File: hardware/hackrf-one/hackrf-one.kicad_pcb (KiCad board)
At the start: 4 copper layers, 120 x 75 mm, 432 parts, among them J1 USB-MICRO-B, J10 GND_CLIP, J2 RF-SHIELD-FRAME, J3 RF-SHIELD-COVER, J4 MOUNTING_HOLE, J5 MOUNTING_HOLE, J6 MOUNTING_HOLE, J7 MOUNTING_HOLE, J8 MOUNTING_HOLE, J9 MOUNTING_HOLE, P1 1V8, P13 GPO1, P14 XCVR_CLKOUT, P15 INTR, P16 CLKIN, P17 GPO6, P18 OEB, P19 GPO3, P2 CLKOUT, P20 GPIO, P21 REF_IN, P22 I2S, P23 DBGEN, P24 TRST, P25 LPC_ISP, P26 LPC_JTAG, P27 MIXER_SDATA, P28 SD, P29 CPLD_JTAG, P3 GND, P30 BANK2_AUX, P31 MIXER_SCLK, P32 MIXER_ENX, P33 MIXER_RESETX, P34 MIX_BYPASS, P35 !MIX_BYPASS, P36 VAA, P37 SCL, P38 SDA, P39 SSP1_SCK, P4 ANTENNA, P40 SSP1_MOSI, P41 SSP1_MISO, P42 TX, P43 RX, P44 HP, P45 LP, P46 TX_MIX_BP, P47 RX_MIX_BP, P48 TX_AMP, P49 RX_AMP, P5 LEDS, P50 AMP_BYPASS, P51 !TX_AMP_PWR, P52 !RX_AMP_PWR, P53 CS_XCVR, P54 CS_AD, P55 TXENABLE, P56 RXENABLE, P57 XTAL2, P58 GCK1, P59 GCK2, P6 GPO4, P60 SGPIO_CLK, P61 DA0, P62 DA7, P63 DD0, P64 DD9, P65 DA4, P66 DD5, P67 RSSI, P68 SPIFI_CS, P69 VREGMODE, P7 GPO2, P70 EN_1V8, P71 ID, P72 GP_CLKIN, P73 P1_2, P74 P1_1, P75 GP_CLKIN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

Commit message: adopt OSHWA convention for SPI signal names
https://www.oshwa.org/a-resolution-to-redefine-spi-signal-names
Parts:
- P40: value SSP1_MOSI -> SSP1_COPI
- P41: value SSP1_MISO -> SSP1_CIPO
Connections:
- net /mcu/usb/power/SPIFI_MISO renamed /mcu/usb/power/SPIFI_CIPO
- net /mcu/usb/power/SPIFI_MOSI renamed /mcu/usb/power/SPIFI_COPI
- net SSP1_MISO renamed SSP1_CIPO
- net SSP1_MOSI renamed SSP1_COPI
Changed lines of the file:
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@@
   (net 145 /mcu/usb/power/SGPIO9)
   (net 146 /mcu/usb/power/SPIFI_CS)
-  (net 147 /mcu/usb/power/SPIFI_MISO)
-  (net 148 /mcu/usb/power/SPIFI_MOSI)
+  (net 147 /mcu/usb/power/SPIFI_CIPO)
+  (net 148 /mcu/usb/power/SPIFI_COPI)
   (net 149 /mcu/usb/power/SPIFI_SCK)
   (net 150 /mcu/usb/power/SPIFI_SIO2)
@@
   (net 210 SDA)
   (net 211 SGPIO_CLK)
-  (net 212 SSP1_MISO)
-  (net 213 SSP1_MOSI)
+  (net 212 SSP1_CIPO)
+  (net 213 SSP1_COPI)
   (net 214 SSP1_SCK)
   (net 215 TX)
@@
     (add_net /mcu/usb/power/SGPIO9)
     (add_net /mcu/usb/power/SPIFI_CS)
-    (add_net /mcu/usb/power/SPIFI_MISO)
-    (add_net /mcu/usb/power/SPIFI_MOSI)
+    (add_net /mcu/usb/power/SPIFI_CIPO)
+    (add_net /mcu/usb/power/SPIFI_COPI)
     (add_net /mcu/usb/power/SPIFI_SCK)
     (add_net /mcu/usb/power/SPIFI_SIO2)
@@
     (add_net SDA)
     (add_net SGPIO_CLK)
-    (add_net SSP1_MISO)
-    (add_net SSP1_MOSI)
+    (add_net SSP1_CIPO)
+    (add_net SSP1_COPI)
     (add_net SSP1_SCK)
     (add_net TX)
@@
       (net 193 GND) (solder_mask_margin 0.1016))
     (pad 1 smd rect (at -0.5334 0 180) (size 0.508 0.5588) (layers C1F F.Paste F.Mask)
-      (net 212 SSP1_MISO) (die_length -2147.483648) (solder_mask_margin 0.1016))
+      (net 212 SSP1_CIPO) (die_length -2147.483648) (solder_mask_margin 0.1016))
   )
   (module hackrf:GSG-0402 (layer C1F)
@@
       (net 99 /mcu/usb/power/I2C1_SDA) (die_length 0.12192))
     (pad 7 thru_hole circle (at -7.62 1.27 180) (size 1.524 1.524) (drill 1.016) (layers *.Cu *.Mask F.SilkS)
-      (net 147 /mcu/usb/power/SPIFI_MISO) (die_length 0.12192))
+      (net 147 /mcu/usb/power/SPIFI_CIPO) (die_length 0.12192))
     (pad 8 thru_hole circle (at -7.62 -1.27 180) (size 1.524 1.524) (drill 1.016) (layers *.Cu *.Mask F.SilkS)
       (net 149 /mcu/usb/power/SPIFI_SCK) (die_length 0.08382))
     (pad 9 thru_hole circle (at -5.08 1.27 180) (size 1.524 1.524) (drill 1.016) (layers *.Cu *.Mask F.SilkS)
-      (net 148 /mcu/usb/power/SPIFI_MOSI) (die_length -2147.483648))
+      (net 148 /mcu/usb/power/SPIFI_COPI) (die_length -2147.483648))
     (pad 10 thru_hole circle (at -5.08 -1.27 180) (size 1.524 1.524) (drill 1.016) (layers *.Cu *.Mask F.SilkS)
       (net 193 GND) (die_length 0.24638))
@@
       (effects (font (size 0.381 0.381) (thickness 0.09652)))
     )
-    (fp_text value SSP1_MOSI (at 0 0) (layer F.SilkS) hide
+    (fp_text value SSP1_COPI (at 0 0) (layer F.SilkS) hide
       (effects (font (size 0.508 0.508) (thickness 0.127)))
     )
     (fp_circle (center 0 0) (end 0.7112 0) (layer F.SilkS) (width 0.2032))
     (pad 1 smd circle (at 0 0) (size 1.27 1.27) (layers C1F F.Mask)
-      (net 213 SSP1_MOSI) (die_length 0.1651))
+      (net 213 SSP1_COPI) (die_length 0.1651))
   )
   (module hackrf:GSG-TESTPOINT-50MIL (layer C1F)
@@
       (effects (font (size 0.381 0.381) (thickness 0.09652)))
     )
-    (fp_text value SSP1_MISO (at 0 0 180) (layer F.SilkS) hide
+    (fp_text value SSP1_CIPO (at 0 0 180) (layer F.SilkS) hide
       (effects (font (size 0.508 0.508) (thickness 0.127)))
     )
     (fp_circle (center 0 0) (end 0.7112 0) (layer F.SilkS) (width 0.2032))
     (pad 1 smd circle (at 0 0 180) (size 1.27 1.27) (layers C1F F.Mask)
-      (net 212 SSP1_MISO) (die_length 0.1651))
+      (net 212 SSP1_CIPO) (die_length 0.1651))
   )
   (module hackrf:GSG-TESTPOINT-50MIL (layer C1F)
@@
       (net 146 /mcu/usb/power/SPIFI_CS) (die_length 0.08382))
     (pad 2 smd rect (at -3.81 -0.635 180) (size 1.905 0.635) (layers C1F F.Paste F.Mask)
-      (net 147 /mcu/usb/power/SPIFI_MISO) (die_length 0.08128))
+      (net 147 /mcu/usb/power/SPIFI_CIPO) (die_length 0.08128))
     (pad 3 smd rect (at -3.81 0.635 180) (size 1.905 0.635) (layers C1F F.Paste F.Mask)
       (net 150 /mcu/usb/power/SPIFI_SIO2) (die_length 0.1143))
@@
       (net 193 GND) (die_length 0.53086))
     (pad 5 smd rect (at 3.81 1.905 180) (size 1.905 0.635) (layers C1F F.Paste F.Mask)
-      (net 148 /mcu/usb/power/SPIFI_MOSI) (die_length -2147.483648))
+      (net 148 /mcu/usb/power/SPIFI_COPI) (die_length -2147.483648))
     (pad 6 smd rect (at 3.81 0.635 180) (size 1.905 0.635) (layers C1F F.Paste F.Mask)
       (net 149 /mcu/usb/power/SPIFI_SCK) (die_length -2147.483648))
@@
       (net 111 /mcu/usb/power/P1_2) (die_length -2147.483648))
     (pad 44 smd rect (at -5.25018 11.00074 315) (size 1.50114 0.29464) (layers C1F F.Paste F.Mask)
-      (net 212 SSP1_MISO) (die_length -2147.483648))
+      (net 212 SSP1_CIPO) (die_length -2147.483648))
     (pad 45 smd rect (at -4.7498 11.00074 315) (size 1.50114 0.29464) (layers C1F F.Paste F.Mask)
       (net 123 /mcu/usb/power/SD_CLK) (die_length 0.01778))
@@
       (net 219 TX_MIX_BP) (die_length 0.01524))
     (pad 47 smd rect (at -3.74904 11.00074 315) (size 1.50114 0.29464) (layers C1F F.Paste F.Mask)
-      (net 213 SSP1_MOSI) (die_length 0.01524))
+      (net 213 SSP1_COPI) (die_length 0.01524))
     (pad 48 smd rect (at -3.2512 11.00074 315) (size 1.50114 0.29464) (layers C1F F.Paste F.Mask)
       (net 129 /mcu/usb/power/SD_POW) (die_length -2147.483648))
@@
       (net 150 /mcu/usb/power/SPIFI_SIO2) (die_length 0.01524))
     (pad 122 smd rect (at 2.25044 -11.00074 315) (size 1.50114 0.29464) (layers C1F F.Paste F.Mask)
-      (net 147 /mcu/usb/power/SPIFI_MISO) (die_length 0.01524))
+      (net 147 /mcu/usb/power/SPIFI_CIPO) (die_length 0.01524))
     (pad 123 smd rect (at 1.75006 -11.00074 315) (size 1.50114 0.29464) (layers C1F F.Paste F.Mask)
-      (net 148 /mcu/usb/power/SPIFI_MOSI) (die_length -2147.483648))
+      (net 148 /mcu/usb/power/SPIFI_COPI) (die_length -2147.483648))
     (pad 124 smd rect (at 1.24968 -11.00074 315) (size 1.50114 0.29464) (layers C1F F.Paste F.Mask)
       (net 146 /mcu/usb/power/SPIFI_CS) (die_length -2147.483648))
@@
       (net 220 VAA))
     (pad 29 smd oval (at 3 0.6 90) (size 0.87 0.245) (layers C1F F.Paste F.Mask)
-      (net 212 SSP1_MISO))
+      (net 212 SSP1_CIPO))
     (pad 30 smd oval (at 3 0.2 90) (size 0.87 0.245) (layers C1F F.Paste F.Mask)
       (net 172 CS_XCVR))
     (pad 31 smd oval (at 3 -0.2 90) (size 0.87 0.245) (layers C1F F.Paste F.Mask)
-      (net 213 SSP1_MOSI))
+      (net 213 SSP1_COPI))
     (pad 32 smd oval (at 3 -0.6 90) (size 0.87 0.245) (layers C1F F.Paste F.Mask)
       (net 203 RSSI))
@@
       (net 220 VAA))
     (pad 34 smd oval (at 3.45 -1.75 90) (size 0.9 0.28) (layers C1F F.Paste F.Mask)
-      (net 213 SSP1_MOSI))
+      (net 213 SSP1_COPI))
     (pad 35 smd oval (at 3.45 -2.25 90) (size 0.9 0.28) (layers C1F F.Paste F.Mask)
       (net 214 SSP1_SCK))

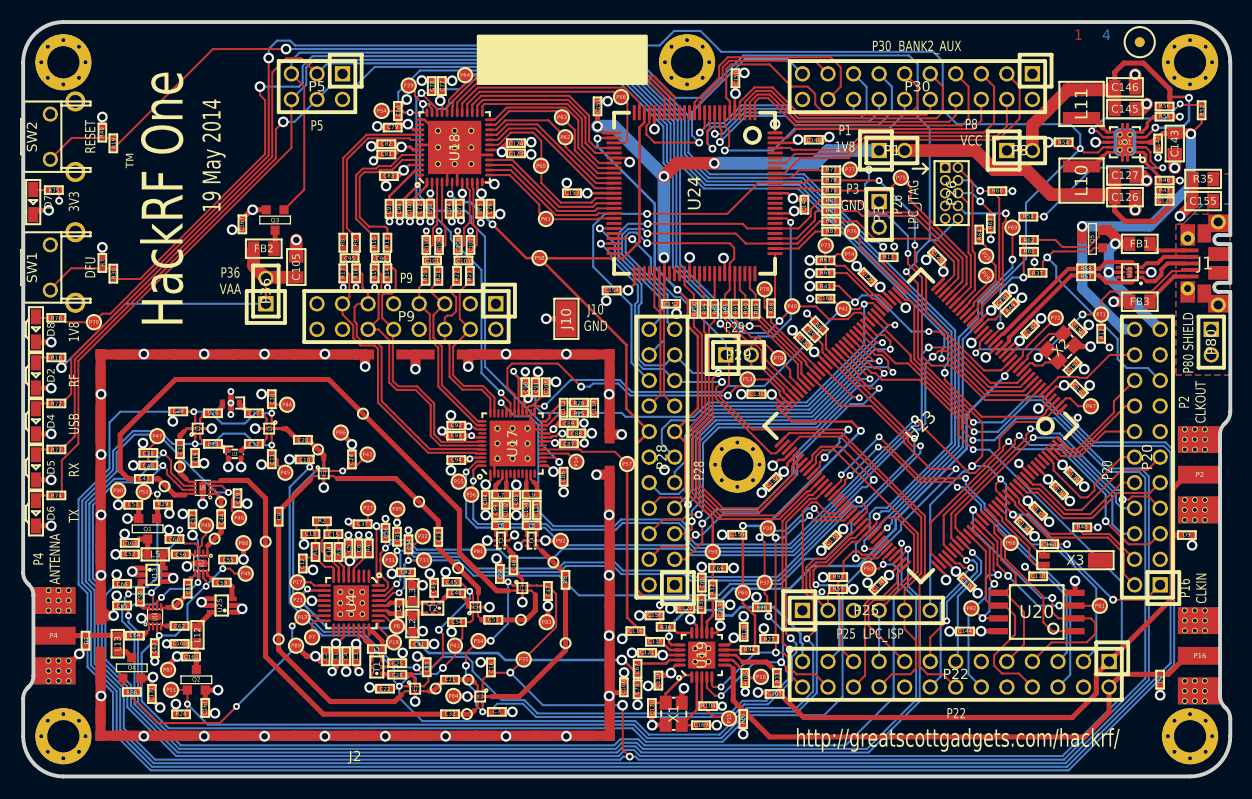
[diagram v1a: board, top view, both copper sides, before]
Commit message: HackRF One: update to KiCad 5.1
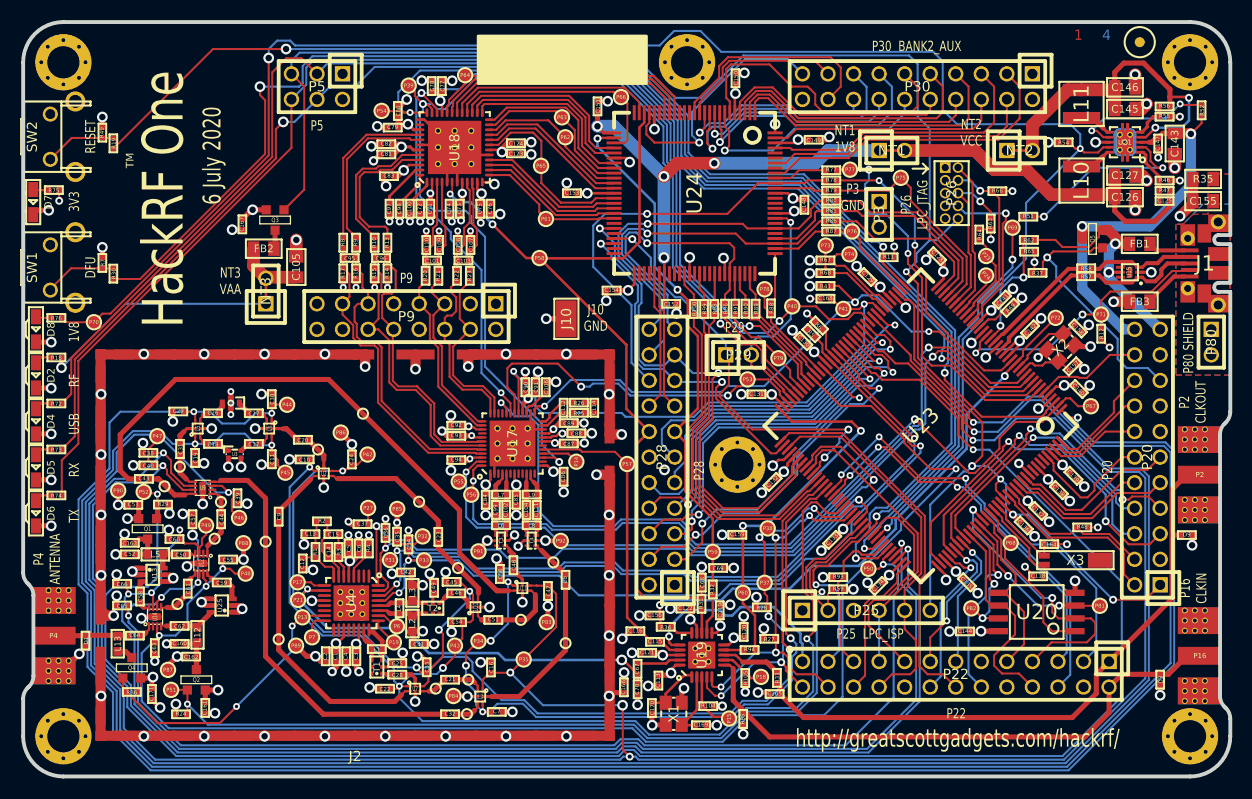
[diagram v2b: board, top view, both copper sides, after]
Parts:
- removed P1: 1V8, hackrf:GSG-HEADER-1x2
- removed P36: VAA, hackrf:GSG-HEADER-1x2
- removed P8: VCC, hackrf:GSG-HEADER-1x2
- added NT1: 1V8, gsg-modules:HEADER-1x2-SHORTED, F.Cu at (146.4, 112.8)
- added NT2: VCC, gsg-modules:HEADER-1x2-SHORTED, F.Cu at (159.1, 112.8)
- added NT3: VAA, gsg-modules:HEADER-1x2-SHORTED, F.Cu at (84.1, 126.7)
- C169, C170: value DNP -> 1.8pF
- Q1, Q2, Q3, Q4, Q5: footprint gsg-modules:SOT23GDS -> gsg-modules:SOT23-3
- U15: value LXES1TBCC2-004 -> TVS
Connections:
- net +1.8V renamed +1V8
- net Net-(C58-Pad1) renamed /frontend/RX_AMP_IN
- P25 pad 3: Net-(P25-Pad3) -> (no net)
- P26 pad 7: Net-(P26-Pad7) -> (no net)
- U12 pad 2: Net-(U12-Pad2) -> (no net)
- U14 pad 2: Net-(U14-Pad2) -> (no net)
- U15 pad 4: Net-(U15-Pad4) -> (no net)
- U15 pad 6: Net-(U15-Pad6) -> (no net)
- U17 pad 12: Net-(U17-Pad12) -> (no net)
- U17 pad 14: Net-(U17-Pad14) -> (no net)
- U17 pad 18: Net-(U17-Pad18) -> (no net)
- U17 pad 3: Net-(U17-Pad3) -> (no net)
- U17 pad 33: Net-(U17-Pad33) -> (no net)
- U17 pad 34: Net-(U17-Pad34) -> (no net)
- U17 pad 40: Net-(U17-Pad40) -> (no net)
- U17 pad 6: Net-(U17-Pad6) -> (no net)
- U17 pad 8: Net-(U17-Pad8) -> (no net)
- U17 pad 9: Net-(U17-Pad9) -> (no net)
- U18 pad 38: Net-(U18-Pad38) -> (no net)
- U23 pad 136: Net-(U23-Pad136) -> (no net)
- U23 pad 138: Net-(U23-Pad138) -> (no net)
- U23 pad 139: Net-(U23-Pad139) -> (no net)
- U23 pad 89: Net-(U23-Pad89) -> (no net)
- U23 pad 90: Net-(U23-Pad90) -> (no net)
- U24 pad 14: Net-(U24-Pad14) -> (no net)
- U24 pad 15: Net-(U24-Pad15) -> (no net)
- U24 pad 16: Net-(U24-Pad16) -> (no net)
- U24 pad 20: Net-(U24-Pad20) -> (no net)
- U24 pad 25: Net-(U24-Pad25) -> (no net)
- U24 pad 44: Net-(U24-Pad44) -> (no net)
- U24 pad 46: Net-(U24-Pad46) -> (no net)
- U24 pad 49: Net-(U24-Pad49) -> (no net)
- U24 pad 50: Net-(U24-Pad50) -> (no net)
- U24 pad 52: Net-(U24-Pad52) -> (no net)
- U24 pad 53: Net-(U24-Pad53) -> (no net)
- U24 pad 54: Net-(U24-Pad54) -> (no net)
- U24 pad 58: Net-(U24-Pad58) -> (no net)
- U24 pad 59: Net-(U24-Pad59) -> (no net)
- U24 pad 60: Net-(U24-Pad60) -> (no net)
- U24 pad 63: Net-(U24-Pad63) -> (no net)
- U24 pad 65: Net-(U24-Pad65) -> (no net)
- U24 pad 66: Net-(U24-Pad66) -> (no net)
- U24 pad 68: Net-(U24-Pad68) -> (no net)
- U24 pad 73: Net-(U24-Pad73) -> (no net)
- U24 pad 75: Net-(U24-Pad75) -> (no net)
- U24 pad 80: Net-(U24-Pad80) -> (no net)
- U24 pad 82: Net-(U24-Pad82) -> (no net)
- U24 pad 85: Net-(U24-Pad85) -> (no net)
- U24 pad 86: Net-(U24-Pad86) -> (no net)
- U24 pad 87: Net-(U24-Pad87) -> (no net)
- U24 pad 93: Net-(U24-Pad93) -> (no net)
- U24 pad 95: Net-(U24-Pad95) -> (no net)
- U24 pad 96: Net-(U24-Pad96) -> (no net)
- U4 pad 1: Net-(U4-Pad1) -> (no net)
- U4 pad 11: Net-(U4-Pad11) -> (no net)
- U4 pad 13: Net-(U4-Pad13) -> (no net)
- U4 pad 14: Net-(U4-Pad14) -> (no net)
- U4 pad 17: Net-(U4-Pad17) -> (no net)
- U4 pad 18: Net-(U4-Pad18) -> (no net)
- U4 pad 2: Net-(U4-Pad2) -> (no net)
- U4 pad 20: Net-(U4-Pad20) -> (no net)
- U4 pad 21: Net-(U4-Pad21) -> (no net)
- U4 pad 3: Net-(U4-Pad3) -> (no net)
- U9 pad 2: Net-(U9-Pad2) -> (no net)
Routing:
- net VCC: track 183.7 -> 181.1 mm
- net Net-(C105-Pad1): track 9.05 -> 6.51 mm
- net +1V8: track 49.8 -> 47.3 mm
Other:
- board text added: "6 July 2020"
- board text added: "NT1 1V8"
- board text added: "NT2 VCC"
- board text added: "NT3 VAA"
- board text removed: "19 May 2014"
- board text removed: "P1 1V8"
- board text removed: "P36 VAA"
- board text removed: "P8 VCC"

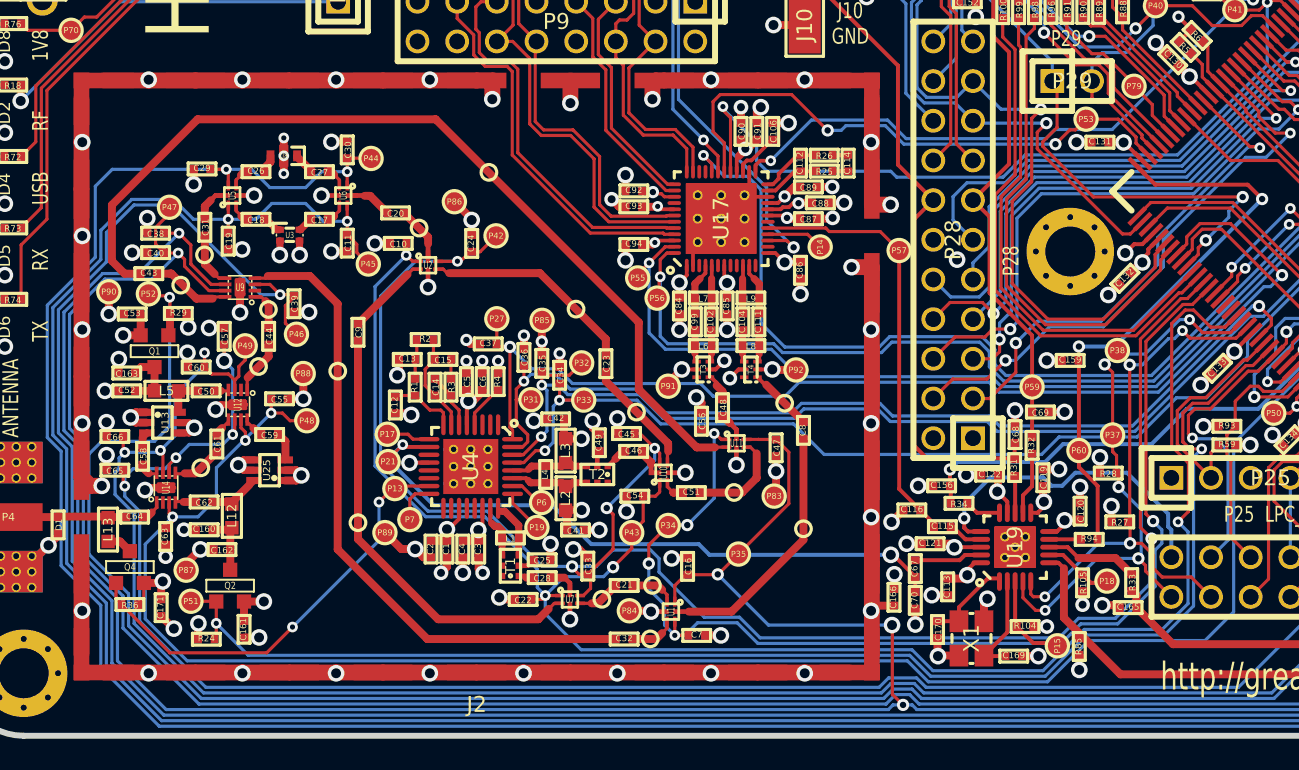
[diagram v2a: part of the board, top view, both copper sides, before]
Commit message: HackRF One: replace obsolete SKY13350-385LF RF switch with SKY13453-385LF
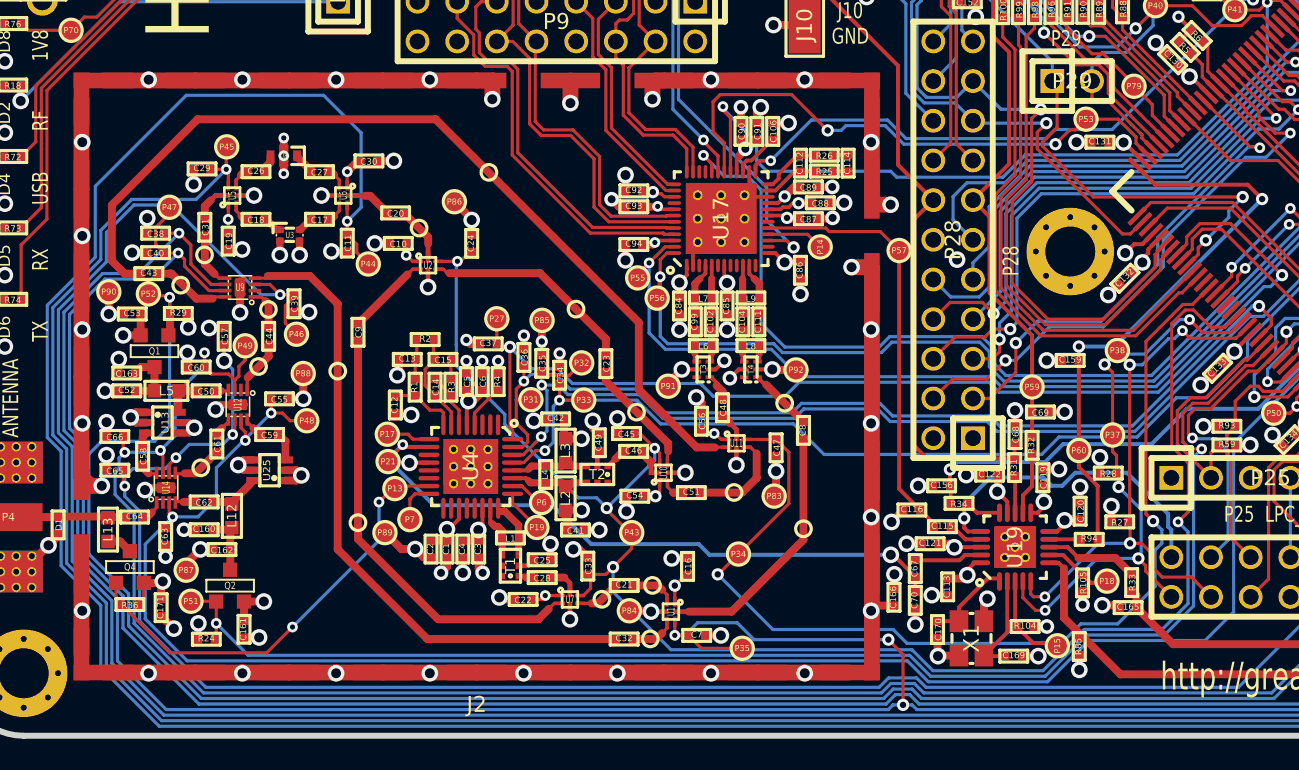
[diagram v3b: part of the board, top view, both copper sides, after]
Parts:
- removed P42: TX, hackrf:GSG-TESTPOINT-50MIL
- C10, C16, C19, C22, C30, C54, C56: value 33pF -> 10nF
- U1, U10, U11, U2, U5, U6, U7: value SKY13350 -> SKY13453; footprint hackrf:GSG-SKY13350-385LF -> gsg-modules:SKY13350-385LF
- moved P45 11.8 mm to (77.0, 137.3)
- moved P44 6.76 mm to (86.1, 144.8)
- moved P35 6.04 mm to (110.0, 169.4)
- moved P34 4.85 mm to (109.8, 163.4)
- moved C30 1.56 mm to (86.1, 138.2), turned to 0 degrees
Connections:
- C10 pad 2: RX -> VAA
- C11 pad 2: LP -> HP
- C16 pad 1: !MIX_BYPASS -> VAA
- C19 pad 2: LP -> VAA
- C22 pad 2: RX -> VAA
- C24 pad 2: TX -> RX
- C29 pad 1: HP -> LP
- C30 pad 1: HP -> VAA
- C33 pad 1: TX -> RX
- C45 pad 2: TX -> RX
- C47 pad 2: !MIX_BYPASS -> MIX_BYPASS
- C54 pad 1: RX -> VAA
- C56 pad 1: MIX_BYPASS -> VAA
- C7 pad 2: MIX_BYPASS -> !MIX_BYPASS
- U1 pad 1: !MIX_BYPASS -> VAA
- U1 pad 5: MIX_BYPASS -> !MIX_BYPASS
- U10 pad 1: RX -> VAA
- U10 pad 5: TX -> RX
- U11 pad 1: MIX_BYPASS -> VAA
- U11 pad 5: !MIX_BYPASS -> MIX_BYPASS
- U2 pad 1: RX -> VAA
- U2 pad 5: TX -> RX
- U23 pad 85: TX -> (no net)
- U5 pad 1: LP -> VAA
- U5 pad 5: HP -> LP
- U6 pad 1: HP -> VAA
- U6 pad 5: LP -> HP
- U7 pad 1: RX -> VAA
- U7 pad 5: TX -> RX
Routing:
- net TX: track 115.0 -> 0.00 mm, vias 5 -> 0
- net VAA: track 92.7 -> 106.0 mm, vias 27 -> 34
- net LP: track 225.5 -> 214.4 mm, vias 3 -> 2
- net !MIX_BYPASS: track 237.4 -> 227.3 mm
- net RX: track 114.9 -> 105.7 mm, vias 4 -> 5
- net MIX_BYPASS: track 74.6 -> 65.9 mm, vias 5 -> 2
- net HP: track 202.5 -> 210.4 mm, vias 3 -> 2
